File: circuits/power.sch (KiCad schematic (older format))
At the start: 3 parts, among them U9 AP2112

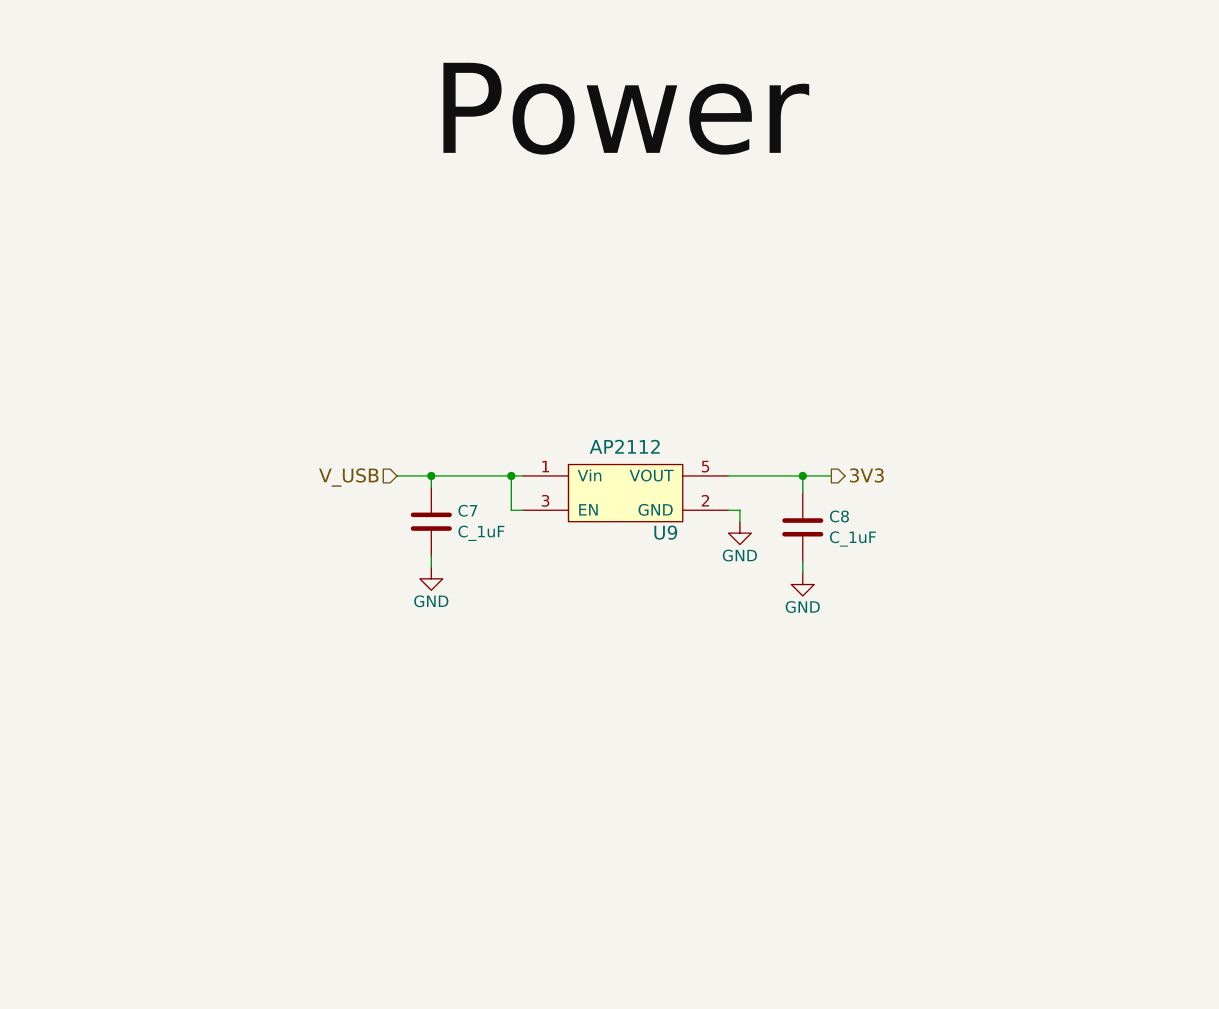
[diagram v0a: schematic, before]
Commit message: sending new board to boardhouse
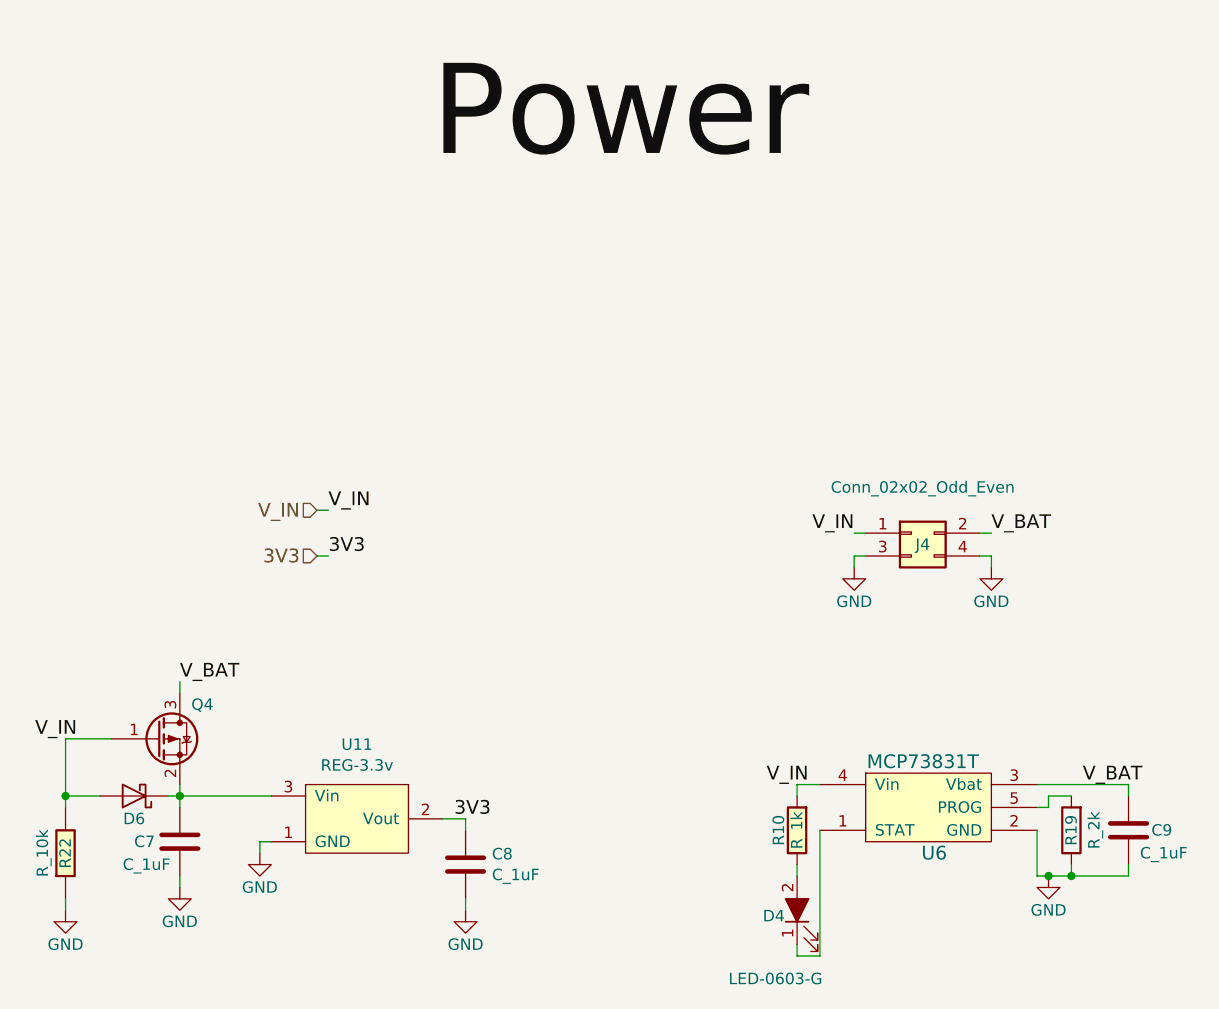
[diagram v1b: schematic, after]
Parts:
- removed U9: AP2112, Package_TO_SOT_SMD:SOT-23-5_HandSoldering, symbol liger-rescue:AP2112
- added C9: C_1uF, Capacitor_SMD:C_0603_1608Metric_Pad1.05x0.95mm_HandSolder, symbol open-automation:C_1uF
- added D3: LED-0603-G, LED_SMD:LED_0603_1608Metric_Pad1.05x0.95mm_HandSolder, symbol open-automation:LED-0603-G
- added D6: D_Schottky-BAT20JFILM, Diode_SMD:D_SOD-323_HandSoldering, symbol open-automation:D_Schottky-BAT20JFILM
- added J4: Conn_02x02_Odd_Even, Connector_PinHeader_2.54mm:PinHeader_2x02_P2.54mm_Vertical_SMD, symbol Connector_Generic:Conn_02x02_Odd_Even
- added Q4: PMOS-DMG3413L, Package_TO_SOT_SMD:SOT-23, symbol open-automation:PMOS-DMG3413L
- added R10: R_1k, Resistor_SMD:R_0603_1608Metric_Pad1.05x0.95mm_HandSolder, symbol open-automation:R_1k
- added R19: R_2k, Resistor_SMD:R_0603_1608Metric_Pad1.05x0.95mm_HandSolder, symbol open-automation:R_2k
- added R22: R_10k, Resistor_SMD:R_0603_1608Metric_Pad1.05x0.95mm_HandSolder, symbol open-automation:R_10K
- added U11: REG-3.3v, Package_TO_SOT_SMD:TO-252-2, symbol open-automation:REG-3.3v
- added U6: MCP73831T, Package_TO_SOT_SMD:SOT-23-5_HandSoldering, symbol open-automation:MCP73831T
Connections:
- net 3V3: now also U11.2 (Vout)
- net GND: now also C9.2, J4.3 (Pin_3), J4.4 (Pin_4), R19.1, R22.1, U11.1 (GND), U6.2 (GND)
- net V_USB: no longer names the net of C7.1
- net V_USB: now also D6.1 (K), Q4.2 (S), U11.3 (Vin)
- new net: D3.2 (A), R10.1
- new net: D3.1 (K), U6.1 (STAT)
- new net: R19.2, U6.5 (PROG)
- new net V_BAT: C9.1, J4.2 (Pin_2), Q4.3 (D), U6.3 (Vbat)
- new net V_IN: D6.2 (A), J4.1 (Pin_1), Q4.1 (G), R10.2, R22.2, U6.4 (Vin)
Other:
- moved on the sheet: C7, C8
